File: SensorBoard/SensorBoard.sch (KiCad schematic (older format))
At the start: 6 parts, among them J1 Conn_01x04_Male, J2 Conn_01x02_Male, U1 JST4Pin, U2 JST4Pin, U3 JST4Pin

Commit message: updated sensor board worked on by olivia ??? changes made
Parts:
- A1: symbol MCU_Module:Arduino_Nano_v3.x -> SensorBoard-rescue:Arduino_Nano_v3.x-MCU_Module
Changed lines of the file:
@@
 EESchema Schematic File Version 4
+LIBS:SensorBoard-cache
 EELAYER 30 0
 EELAYER END
@@
 $EndDescr
 $Comp
-L MCU_Module:Arduino_Nano_v3.x A1
+L SensorBoard-rescue:Arduino_Nano_v3.x-MCU_Module A1
 U 1 1 5E27973B
 P 4300 4400

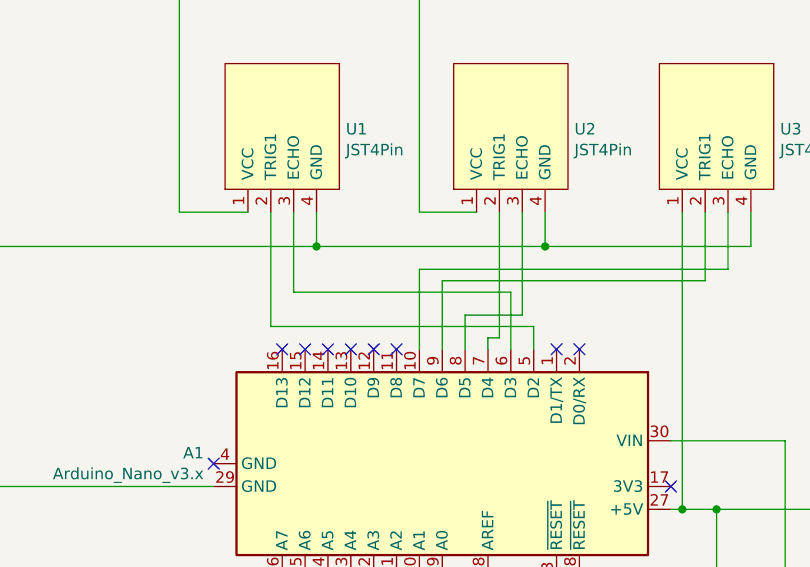
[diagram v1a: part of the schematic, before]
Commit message: switched pins on ultrasonic to PWM pins and switched some wiring
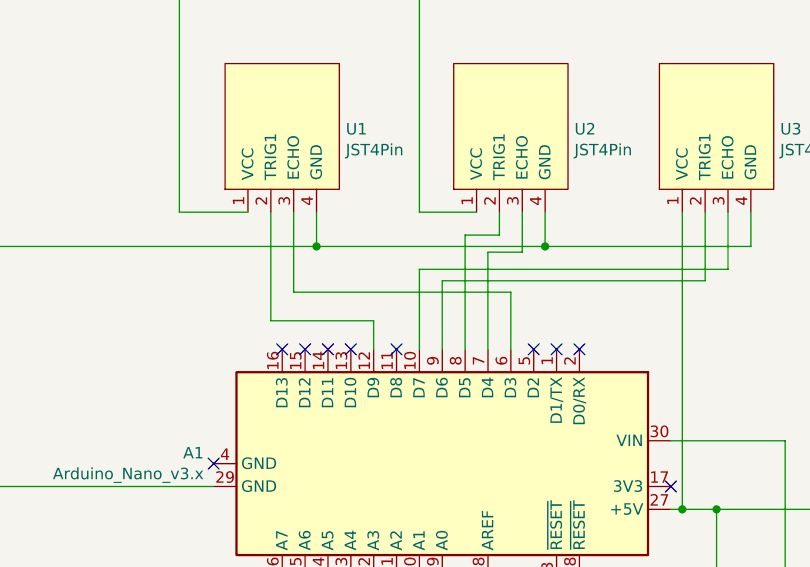
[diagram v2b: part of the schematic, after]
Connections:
- net at A1.12 (D9): now also U1.2 (TRIG1)
- net at A1.5 (D2): no longer U1.2 (TRIG1)
- net at A1.7 (D4): now also U2.3 (ECHO); no longer U2.2 (TRIG1)
- net at A1.8 (D5): now also U2.2 (TRIG1); no longer U2.3 (ECHO)
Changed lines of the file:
@@
 Connection ~ 4750 3450
-Wire Wire Line
-	3550 3300 3550 3800
-Wire Wire Line
-	3550 3800 4700 3800
-Wire Wire Line
-	4700 3800 4700 3900
 Wire Wire Line
 	3650 3300 3650 3650
@@
 Wire Wire Line
 	4600 3650 4600 3900
-Wire Wire Line
-	4550 3300 4550 3850
-Wire Wire Line
-	4550 3850 4500 3850
-Wire Wire Line
-	4500 3850 4500 3900
-Wire Wire Line
-	4650 3300 4650 3750
-Wire Wire Line
-	4650 3750 4400 3750
-Wire Wire Line
-	4400 3750 4400 3900
 Wire Wire Line
 	5450 3300 5450 3600
@@
 NoConn ~ 4800 3900
 NoConn ~ 4100 3900
-NoConn ~ 4000 3900
 NoConn ~ 3900 3900
 NoConn ~ 3800 3900
 NoConn ~ 3700 3900
 NoConn ~ 3600 3900
+Wire Wire Line
+	4400 3900 4400 3400
+Wire Wire Line
+	4400 3400 4550 3400
+Wire Wire Line
+	4550 3400 4550 3300
+Wire Wire Line
+	4500 3900 4500 3475
+Wire Wire Line
+	4500 3475 4650 3475
+Wire Wire Line
+	4650 3475 4650 3300
+Wire Wire Line
+	3550 3300 3550 3775
+Wire Wire Line
+	3550 3775 4000 3775
+Wire Wire Line
+	4000 3775 4000 3900
+NoConn ~ 4700 3900
 $EndSCHEMATC
